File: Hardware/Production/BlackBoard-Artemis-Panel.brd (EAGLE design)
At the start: 167.6 x 120.9 mm, 522 parts, among them IC1 LM1117, IC2 LM1117, IC3 LM1117, IC4 LM1117, J10 CORTEX_DEBUG, J13 POWER_JACKTOE, J15 USB-C, J16 CORTEX_DEBUG, J19 POWER_JACKTOE, J2 CORTEX_DEBUG, J21 USB-C, J22 CORTEX_DEBUG, J3 POWER_JACKTOE, J5 USB-C, J6 POWER_JACKTOE, J9 USB-C, Q1 1.1A/60V/600mΩ, Q2 1.1A/60V/600mΩ, Q3 1.1A/60V/600mΩ, Q4 1.1A/60V/600mΩ, U1 AP2112-3.3V, U10 AP2112-3.3V, U11 CH340C, U12 ARTEMIS_MODULESMD, U2 CH340C, U3 AP2112-3.3V, U4 ARTEMIS_MODULESMD, U5 CH340C, U6 ARTEMIS_MODULESMD, U7 AP2112-3.3V, U8 CH340C, U9 ARTEMIS_MODULESMD, Y1 32.768kHz, Y2 32.768kHz, Y3 32.768kHz, Y4 32.768kHz

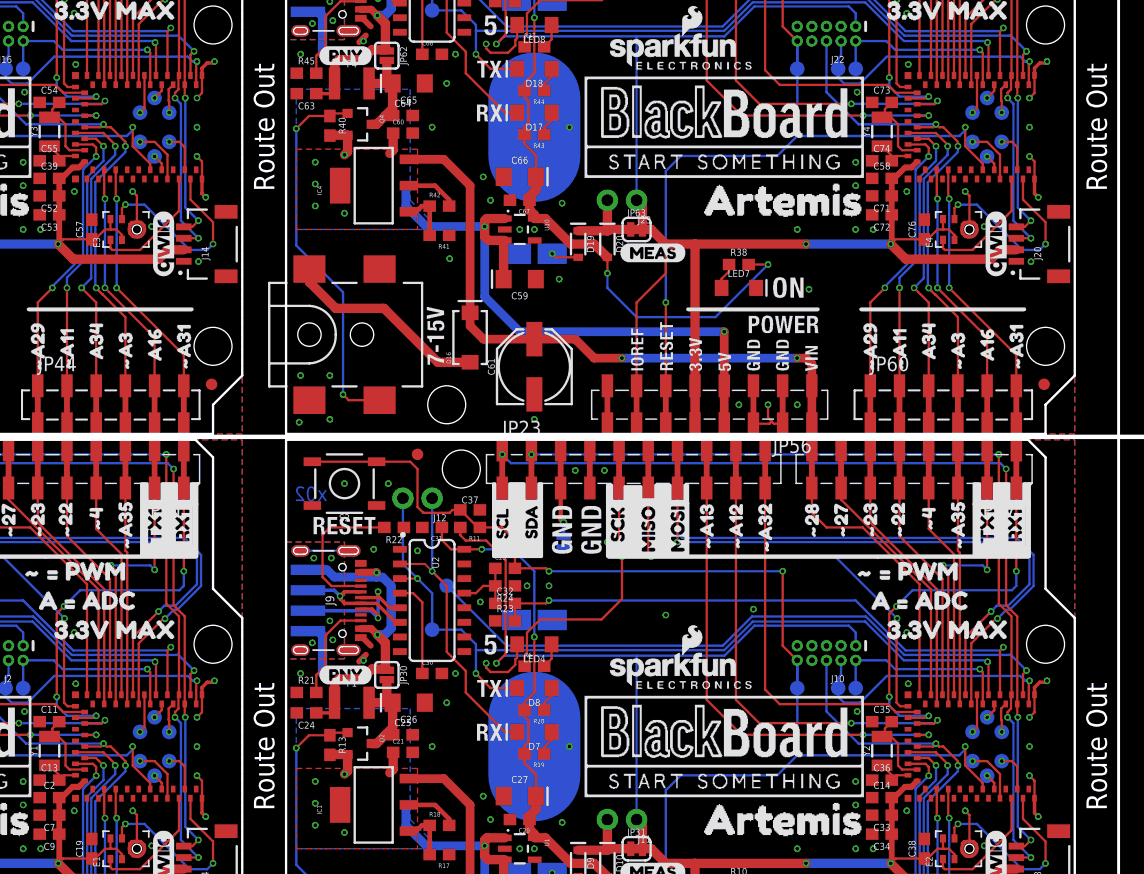
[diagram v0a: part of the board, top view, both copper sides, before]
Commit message: Update silk on Artemis FP
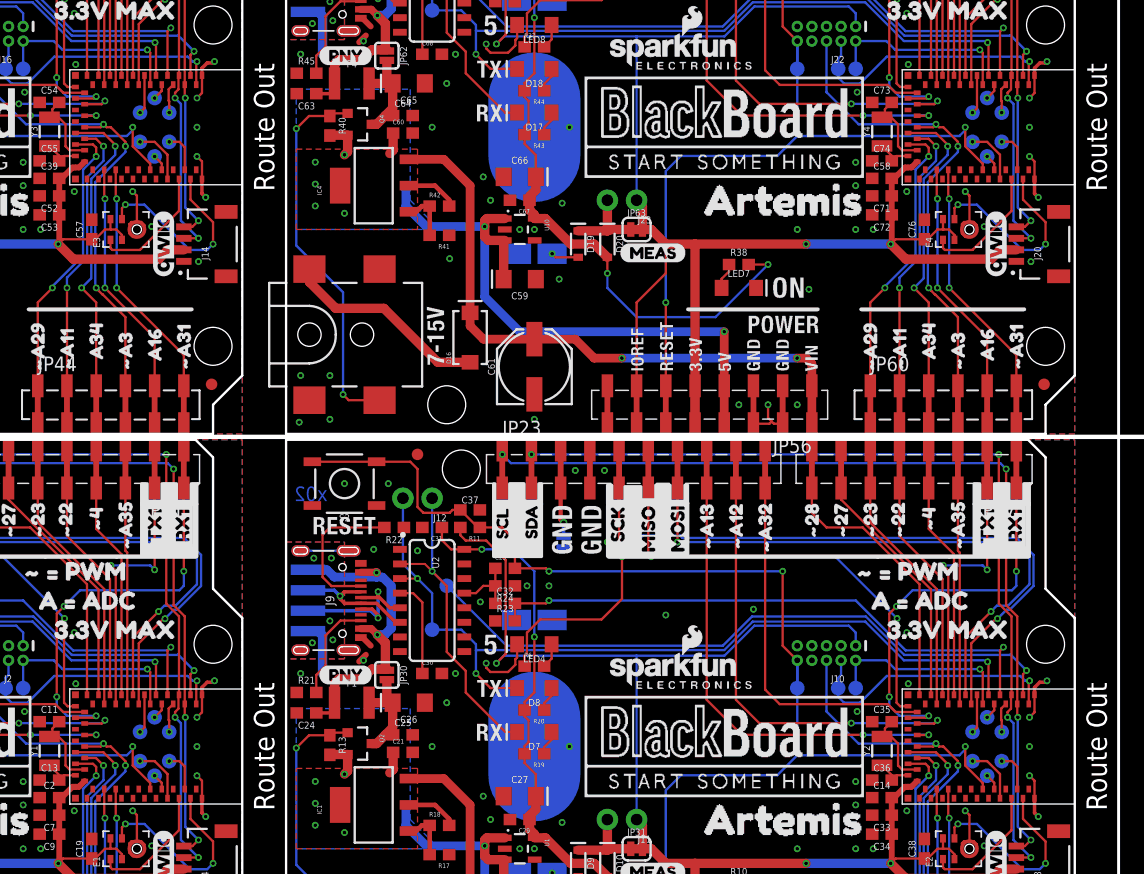
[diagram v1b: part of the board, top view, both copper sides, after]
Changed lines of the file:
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@@
 <layer number="23" name="tOrigins" color="15" fill="1" visible="yes" active="yes"/>
 <layer number="24" name="bOrigins" color="15" fill="1" visible="yes" active="yes"/>
-<layer number="25" name="tNames" color="7" fill="1" visible="yes" active="yes"/>
-<layer number="26" name="bNames" color="7" fill="1" visible="yes" active="yes"/>
-<layer number="27" name="tValues" color="7" fill="1" visible="yes" active="yes"/>
-<layer number="28" name="bValues" color="7" fill="1" visible="yes" active="yes"/>
-<layer number="29" name="tStop" color="7" fill="3" visible="yes" active="yes"/>
-<layer number="30" name="bStop" color="7" fill="6" visible="yes" active="yes"/>
-<layer number="31" name="tCream" color="7" fill="4" visible="yes" active="yes"/>
-<layer number="32" name="bCream" color="7" fill="5" visible="yes" active="yes"/>
-<layer number="33" name="tFinish" color="6" fill="3" visible="yes" active="yes"/>
-<layer number="34" name="bFinish" color="6" fill="6" visible="yes" active="yes"/>
-<layer number="35" name="tGlue" color="7" fill="4" visible="yes" active="yes"/>
-<layer number="36" name="bGlue" color="7" fill="5" visible="yes" active="yes"/>
-<layer number="37" name="tTest" color="7" fill="1" visible="yes" active="yes"/>
-<layer number="38" name="bTest" color="7" fill="1" visible="yes" active="yes"/>
-<layer number="39" name="tKeepout" color="4" fill="11" visible="yes" active="yes"/>
-<layer number="40" name="bKeepout" color="1" fill="11" visible="yes" active="yes"/>
-<layer number="41" name="tRestrict" color="4" fill="10" visible="yes" active="yes"/>
-<layer number="42" name="bRestrict" color="1" fill="10" visible="yes" active="yes"/>
-<layer number="43" name="vRestrict" color="2" fill="10" visible="yes" active="yes"/>
-<layer number="44" name="Drills" color="7" fill="1" visible="yes" active="yes"/>
+<layer number="25" name="tNames" color="7" fill="1" visible="no" active="yes"/>
+<layer number="26" name="bNames" color="7" fill="1" visible="no" active="yes"/>
+<layer number="27" name="tValues" color="7" fill="1" visible="no" active="yes"/>
+<layer number="28" name="bValues" color="7" fill="1" visible="no" active="yes"/>
+<layer number="29" name="tStop" color="7" fill="3" visible="no" active="yes"/>
+<layer number="30" name="bStop" color="7" fill="6" visible="no" active="yes"/>
+<layer number="31" name="tCream" color="7" fill="4" visible="no" active="yes"/>
+<layer number="32" name="bCream" color="7" fill="5" visible="no" active="yes"/>
+<layer number="33" name="tFinish" color="6" fill="3" visible="no" active="yes"/>
+<layer number="34" name="bFinish" color="6" fill="6" visible="no" active="yes"/>
+<layer number="35" name="tGlue" color="7" fill="4" visible="no" active="yes"/>
+<layer number="36" name="bGlue" color="7" fill="5" visible="no" active="yes"/>
+<layer number="37" name="tTest" color="7" fill="1" visible="no" active="yes"/>
+<layer number="38" name="bTest" color="7" fill="1" visible="no" active="yes"/>
+<layer number="39" name="tKeepout" color="4" fill="11" visible="no" active="yes"/>
+<layer number="40" name="bKeepout" color="1" fill="11" visible="no" active="yes"/>
+<layer number="41" name="tRestrict" color="4" fill="10" visible="no" active="yes"/>
+<layer number="42" name="bRestrict" color="1" fill="10" visible="no" active="yes"/>
+<layer number="43" name="vRestrict" color="2" fill="10" visible="no" active="yes"/>
+<layer number="44" name="Drills" color="7" fill="1" visible="no" active="yes"/>
 <layer number="45" name="Holes" color="7" fill="1" visible="yes" active="yes"/>
-<layer number="46" name="Milling" color="3" fill="1" visible="yes" active="yes"/>
-<layer number="47" name="Measures" color="7" fill="1" visible="yes" active="yes"/>
-<layer number="48" name="Document" color="7" fill="1" visible="yes" active="yes"/>
+<layer number="46" name="Milling" color="3" fill="1" visible="no" active="yes"/>
+<layer number="47" name="Measures" color="7" fill="1" visible="no" active="yes"/>
+<layer number="48" name="Document" color="7" fill="1" visible="no" active="yes"/>
 <layer number="49" name="Reference" color="7" fill="1" visible="yes" active="yes"/>
-<layer number="50" name="ReferenceLS" color="12" fill="1" visible="yes" active="yes"/>
+<layer number="50" name="ReferenceLS" color="12" fill="1" visible="no" active="yes"/>
 <layer number="51" name="tDocu" color="6" fill="1" visible="yes" active="yes"/>
-<layer number="52" name="bDocu" color="7" fill="1" visible="yes" active="yes"/>
+<layer number="52" name="bDocu" color="7" fill="1" visible="no" active="yes"/>
 <layer number="53" name="tGND_GNDA" color="7" fill="1" visible="no" active="no"/>
 <layer number="54" name="bGND_GNDA" color="7" fill="1" visible="no" active="no"/>

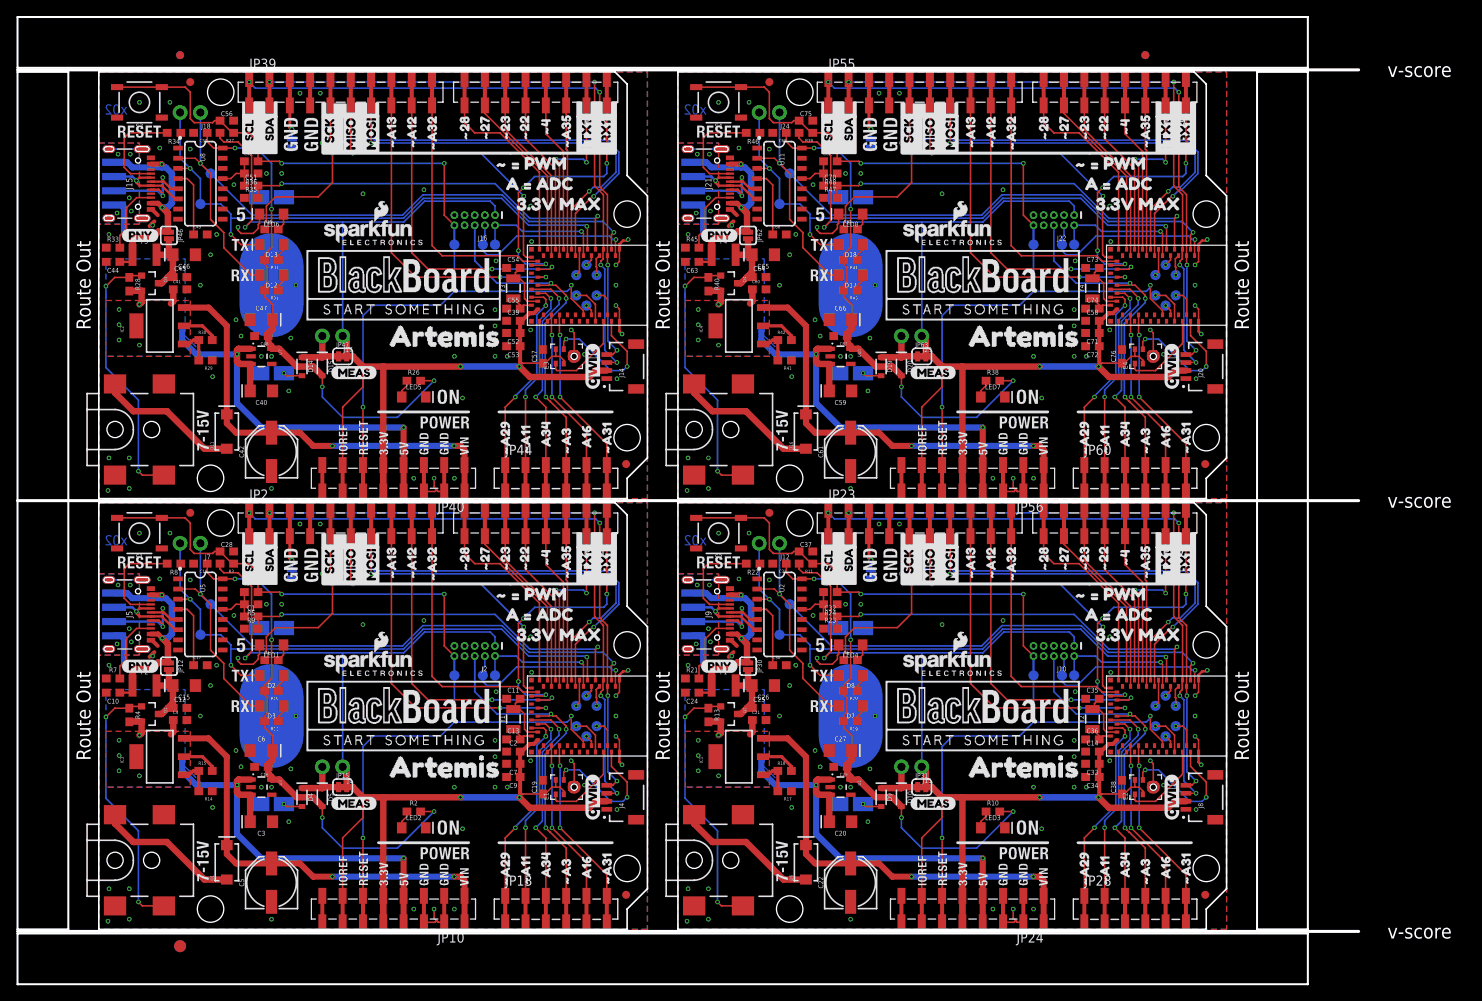
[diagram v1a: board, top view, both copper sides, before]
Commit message: Adding production panel
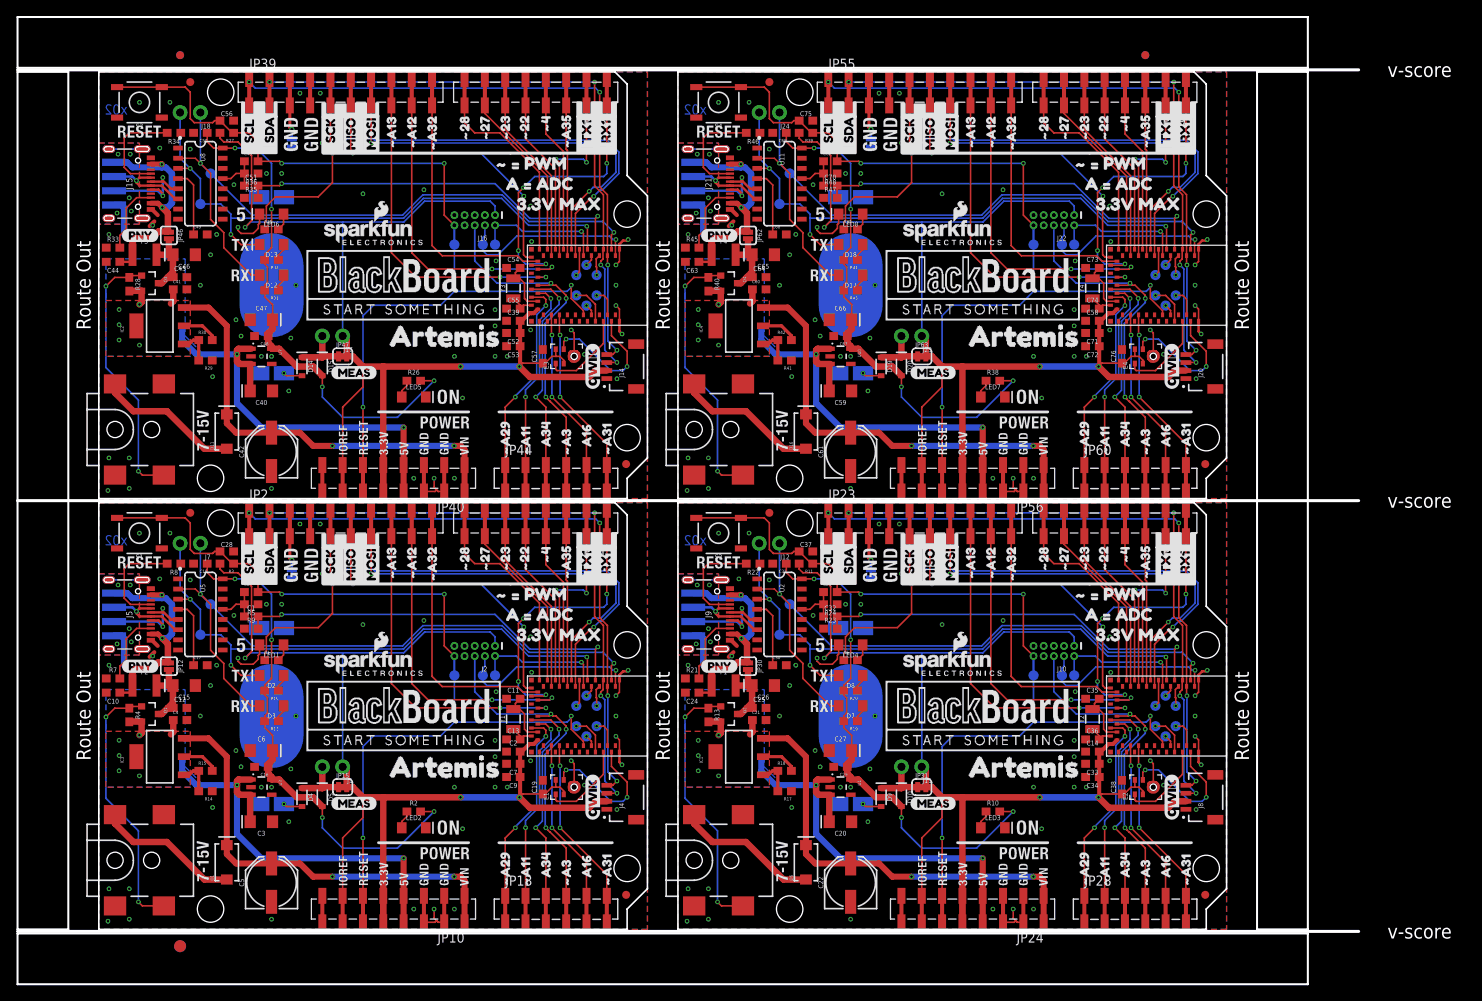
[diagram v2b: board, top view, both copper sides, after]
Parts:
- U$125, U$172, U$78: device buzzard_labels (10):SCL3 -> buzzard_labels (1):#425
- U$126, U$173, U$79: device buzzard_labels (10):SDA4 -> buzzard_labels (1):#434
- U$127, U$174, U$80: device buzzard_labels (1):#425 -> buzzard_labels (1):80
- U$128, U$175, U$81: device buzzard_labels (1):#434 -> buzzard_labels (1):91
- U$129, U$176, U$82: device buzzard_labels (1):80 -> buzzard_labels (1):102
- U$130, U$177, U$83: device buzzard_labels (1):91 -> buzzard_labels (1):383
- U$131, U$178, U$84: device buzzard_labels (1):102 -> buzzard_labels (2):#_#_PWM7
- U$132, U$179, U$85: device buzzard_labels (1):383 -> buzzard_labels (2):3#3V_MAX2
- U$133, U$180, U$86: device buzzard_labels (2):#_#_PWM7 -> buzzard_labels (2):A_#_ADC6
- U$134, U$181, U$87: device buzzard_labels (2):3#3V_MAX2 -> buzzard_labels (2):MEAS3
- U$135, U$182, U$88: device buzzard_labels (2):A_#_ADC6 -> buzzard_labels (2):RX11
- U$136, U$183, U$89: device buzzard_labels (2):MEAS3 -> buzzard_labels (2):TX10
- U$137, U$184, U$90: device buzzard_labels (2):RX11 -> buzzard_labels (3):RX01
- U$138, U$185, U$91: device buzzard_labels (2):TX10 -> buzzard_labels (3):TX00
- U$139, U$186, U$92: device buzzard_labels (3):RX01 -> buzzard_labels (5):AREF2
- U$140, U$187, U$93: device buzzard_labels (3):TX00 -> buzzard_labels (6):SCL1
- U$141, U$188, U$94: device buzzard_labels (5):AREF2 -> buzzard_labels (6):SDA0
- U$18: device Labels:QWIIC_COPYRIGHT_SMALL -> buzzard_labels (6):SCL1
- U$22: device buzzard_labels (13):G1 -> buzzard_labels (6):SDA0
- U$23: device buzzard_labels (13):V0 -> Labels:QWIIC_COPYRIGHT_SMALL
- U$24: device buzzard_labels (14):D#3 -> buzzard_labels (13):G1
- U$32: device buzzard_labels (14):D#4 -> buzzard_labels (13):V0
- U$37: device buzzard_labels:PNY0 -> buzzard_labels (14):D#3
- U$39: device buzzard_labels (3):ARTEMIS0 -> buzzard_labels (14):D#4
- U$40: device buzzard_labels (3):ARTEMIS0 -> buzzard_labels:PNY0
- U$41: device buzzard_labels:A160 -> buzzard_labels (3):ARTEMIS0
- U$42: device buzzard_labels (1):#48 -> buzzard_labels (3):ARTEMIS0
- U$43: device buzzard_labels (1):#229 -> buzzard_labels:A160
- U$44: device buzzard_labels (1):#2310 -> buzzard_labels (1):#48
- U$45: device buzzard_labels (1):#2711 -> buzzard_labels (1):#229
- U$46: device buzzard_labels (1):#2812 -> buzzard_labels (1):#2310
- U$51: device buzzard_labels (1):#A31 -> buzzard_labels (1):#2711
- U$52: device buzzard_labels (1):#A113 -> buzzard_labels (1):#2812
- U$54: device buzzard_labels (1):#A294 -> buzzard_labels (1):#A31
- U$55: device buzzard_labels (1):#A310 -> buzzard_labels (1):#A113
- U$56: device buzzard_labels (1):#A357 -> buzzard_labels (1):#A294
- U$57: device buzzard_labels (10):SCL3 -> buzzard_labels (1):#A310
- U$58: device buzzard_labels (10):SDA4 -> buzzard_labels (1):#A357
- moved U$57 123.5 mm to (135.9, 4.45)
- moved U$18 118.4 mm to (18.8, 43.4)
- moved U$58 109.5 mm to (130.8, 42.8)
- moved U$23 61.8 mm to (134.1, 16.5), flipped to the top, turned to 90 degrees
- moved U$22 56.9 mm to (21.3, 43.4), flipped to the top, turned to 90 degrees
- moved U$40 52.6 mm to (75.2, 32.9), flipped to the top
- moved U$138 50.8 mm to (10.2, 96.3), flipped to the bottom
- moved U$185 50.8 mm to (82.5, 96.3), flipped to the bottom
- moved U$91 50.8 mm to (82.5, 42.4), flipped to the bottom
- moved U$137 50.7 mm to (12.7, 96.3), flipped to the bottom
- moved U$184 50.7 mm to (85.1, 96.3), flipped to the bottom
- moved U$90 50.7 mm to (85.1, 42.4), flipped to the bottom
- moved U$126 47.0 mm to (63.2, 76.3), flipped to the bottom, turned to 0 degrees
- moved U$173 47.0 mm to (135.6, 76.3), flipped to the bottom, turned to 0 degrees
- moved U$79 47.0 mm to (135.6, 22.5), flipped to the bottom, turned to 0 degrees
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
